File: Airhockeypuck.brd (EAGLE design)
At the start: 80 x 80 mm, 22 parts, among them J1 USB-MB-H

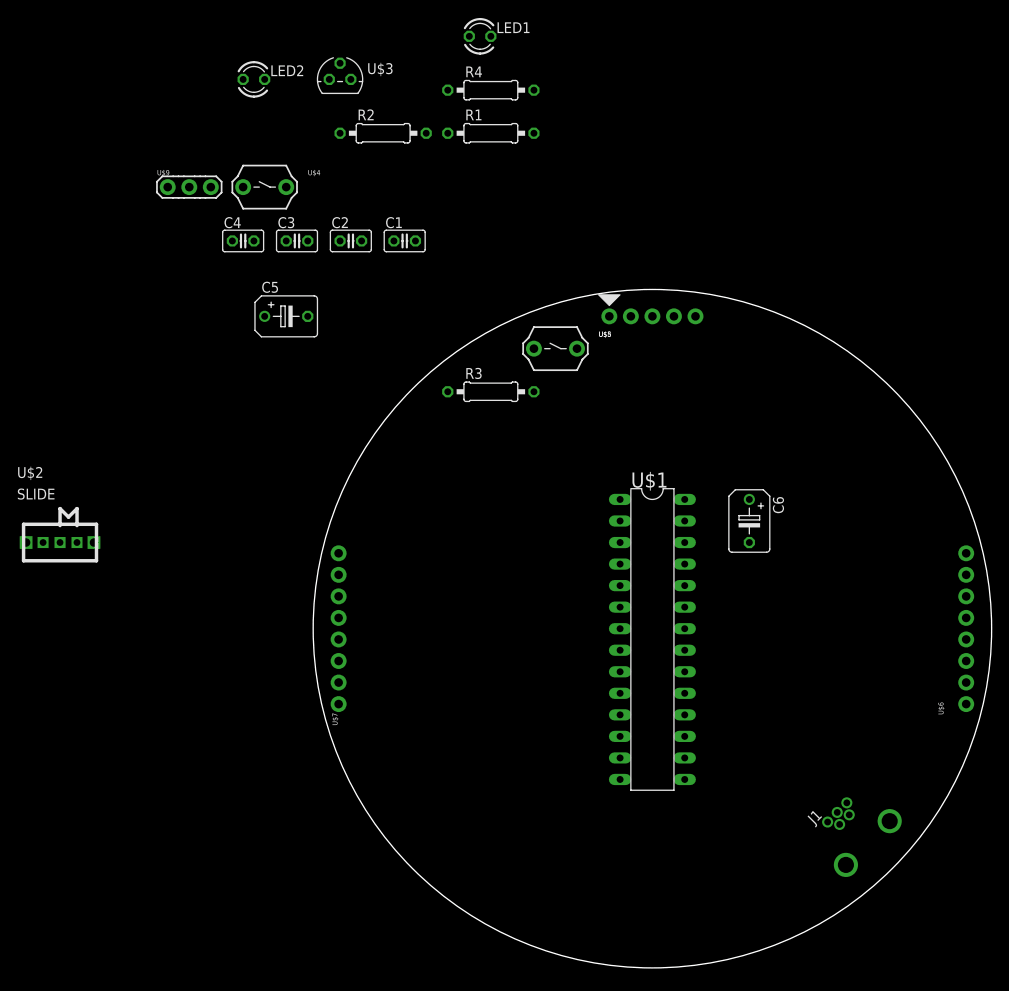
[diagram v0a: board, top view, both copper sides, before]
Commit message: Created IMU part and added into PCB design
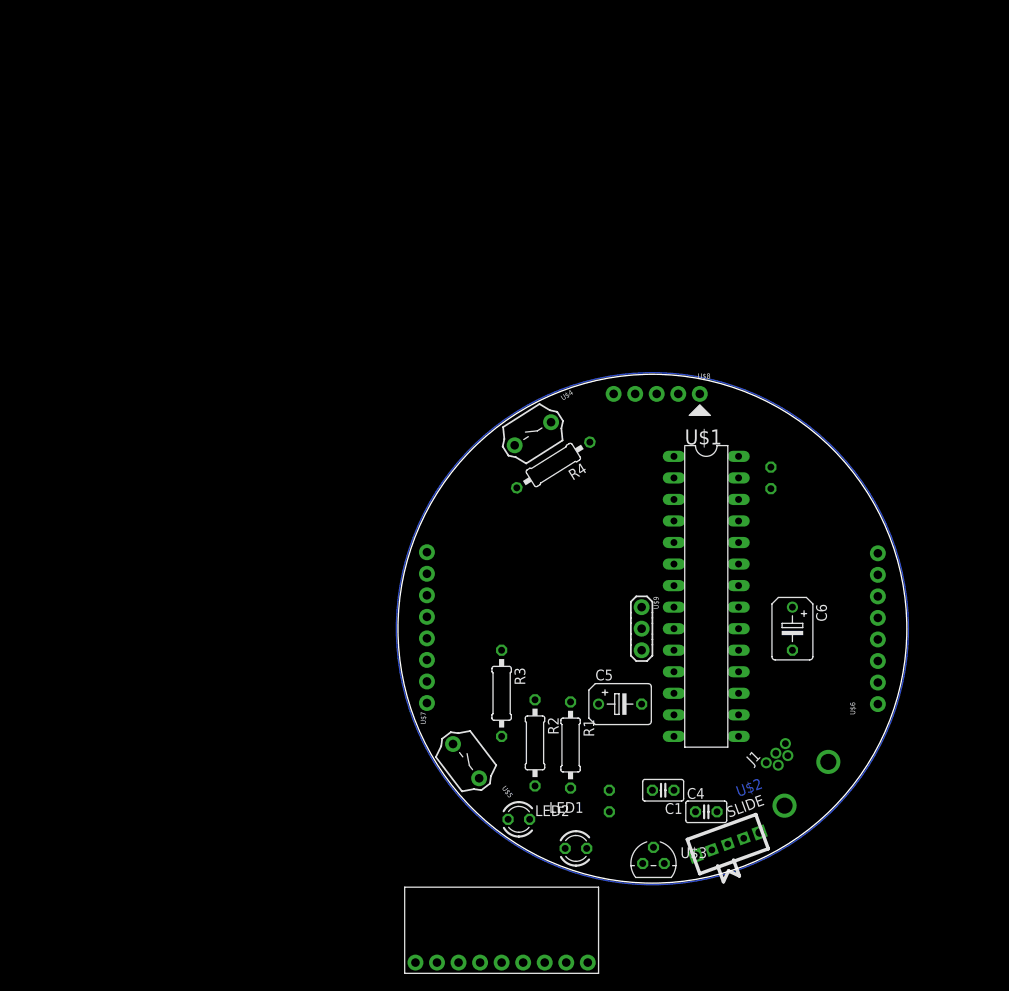
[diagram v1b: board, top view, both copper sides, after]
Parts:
- added U$10: IMU, MEE_433:IMU
- moved U$3 99.6 mm to (0.13, -26.4)
- moved LED1 96.4 mm to (-9.02, -24.6)
- moved LED2 92.7 mm to (-15.7, -21.2)
- moved C4 86.7 mm to (6.35, -20.3)
- moved U$2 86.4 mm to (8.89, -24.1), turned to 200 degrees
- moved U$9 74.5 mm to (-1.27, 1.27), turned to 270 degrees
- moved R2 74.1 mm to (-13.8, -12.2), turned to 270 degrees
- moved R1 72.7 mm to (-9.65, -12.4), turned to 270 degrees
- moved C2 72.7 mm to (-5.08, -19.1), flipped to the bottom, turned to 90 degrees
- moved C1 71.6 mm to (1.27, -17.8), turned to 180 degrees
- moved C3 62.5 mm to (14.0, 19.1), flipped to the bottom, turned to 270 degrees
- moved C5 60.3 mm to (-3.81, -7.62)
- moved U$5 49.8 mm to (-22.0, -14.4), turned to 307.3 degrees
- moved R4 44.8 mm to (-11.7, 20.6), turned to 212 degrees
- moved U$4 43.0 mm to (-14.1, 24.3), turned to 32.4 degrees
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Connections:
- net +5V: now also U$2.2
- net N$1: now also U$2.3; no longer U$2.2
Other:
- board size 80 x 80 mm -> 60 x 60 mm

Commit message: minor edits
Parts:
- moved U$10 51.1 mm to (-1.02, 5.33), turned to 90 degrees
- moved U$9 1.27 mm to (-1.27, 0.00)
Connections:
- net +3V3: now also U$10.2.
- net B2: now also U$10.4.
- net B3: now also U$10.5.
- net GND: now also U$10.3.
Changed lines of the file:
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@@
 <attribute name="VALUE" x="6.858" y="32.258" size="0.6096" layer="27" font="vector" ratio="20" rot="R180"/>
 </element>
-<element name="U$9" library="MEE_433" package="OSC" value="8MHz" x="-1.27" y="1.27" smashed="yes" rot="R270">
-<attribute name="NAME" x="0.127" y="5.08" size="0.6096" layer="25" font="vector" ratio="20" rot="R270"/>
-<attribute name="VALUE" x="-3.302" y="5.08" size="0.6096" layer="27" font="vector" ratio="20" rot="R270"/>
+<element name="U$9" library="MEE_433" package="OSC" value="8MHz" x="-1.27" y="0" smashed="yes" rot="R270">
+<attribute name="NAME" x="0.127" y="3.81" size="0.6096" layer="25" font="vector" ratio="20" rot="R270"/>
+<attribute name="VALUE" x="-3.302" y="3.81" size="0.6096" layer="27" font="vector" ratio="20" rot="R270"/>
 </element>
-<element name="U$10" library="MEE_433" package="IMU" value="IMU" x="-27.94" y="-38.1" smashed="yes"/>
+<element name="U$10" library="MEE_433" package="IMU" value="IMU" x="-1.016" y="5.334" smashed="yes" rot="R90"/>
 </elements>
 <signals>
@@
 <contactref element="U$6" pad="1"/>
 <contactref element="U$7" pad="1"/>
+<contactref element="U$10" pad="3."/>
 <wire x1="-26.586" y1="-7.493" x2="-20.4317875" y2="-16.3715" width="0" layer="19" extent="1-1"/>
 <wire x1="-13.843" y1="-7.112" x2="-20.4317875" y2="-16.3715" width="0" layer="19" extent="1-1"/>
 <wire x1="-9.652" y1="-7.366" x2="-13.843" y2="-7.112" width="0" layer="19" extent="1-1"/>
 <wire x1="-1.27" y1="-7.62" x2="-9.652" y2="-7.366" width="0" layer="19" extent="1-1"/>
-<wire x1="-1.27" y1="1.27" x2="-1.27" y2="-7.62" width="0" layer="19" extent="1-1"/>
-<wire x1="2.54" y1="3.81" x2="-1.27" y2="1.27" width="0" layer="19" extent="1-1"/>
+<wire x1="-1.27" y1="0" x2="-1.27" y2="-7.62" width="0" layer="19" extent="1-1"/>
+<wire x1="2.54" y1="3.81" x2="-1.27" y2="0" width="0" layer="19" extent="1-1"/>
+<wire x1="-1.016" y1="10.414" x2="2.54" y2="3.81" width="0" layer="19" extent="1-1"/>
 <wire x1="10.16" y1="-1.27" x2="2.54" y2="3.81" width="0" layer="19" extent="1-1"/>
 <wire x1="16.51" y1="-1.27" x2="10.16" y2="-1.27" width="0" layer="19" extent="1-1"/>
@@
 <wire x1="-1.143" y1="-26.416" x2="0" y2="-17.78" width="0" layer="19" extent="1-1"/>
 <wire x1="26.586" y1="-7.62" x2="16.51" y2="-1.27" width="0" layer="19" extent="1-1"/>
-<wire x1="10.16" y1="19.05" x2="2.54" y2="3.81" width="0" layer="19" extent="1-1"/>
+<wire x1="10.16" y1="19.05" x2="-1.016" y2="10.414" width="0" layer="19" extent="1-1"/>
 <wire x1="13.97" y1="17.78" x2="10.16" y2="19.05" width="0" layer="19" extent="1-1"/>
 <wire x1="0.508" y1="28.956" x2="10.16" y2="19.05" width="0" layer="19" extent="1-1"/>
@@
 <contactref element="R3" pad="1"/>
 <contactref element="U$7" pad="2"/>
+<contactref element="U$10" pad="2."/>
 <wire x1="10.16" y1="21.59" x2="13.97" y2="20.32" width="0" layer="19" extent="1-1"/>
 <wire x1="3.048" y1="28.956" x2="10.16" y2="21.59" width="0" layer="19" extent="1-1"/>
@@
 <wire x1="10.16" y1="8.89" x2="13.97" y2="20.32" width="0" layer="19" extent="1-1"/>
 <wire x1="16.51" y1="3.81" x2="10.16" y2="8.89" width="0" layer="19" extent="1-1"/>
-<wire x1="2.54" y1="-8.89" x2="16.51" y2="3.81" width="0" layer="19" extent="1-1"/>
+<wire x1="-1.016" y1="7.874" x2="10.16" y2="8.89" width="0" layer="19" extent="1-1"/>
+<wire x1="2.54" y1="-8.89" x2="-1.016" y2="7.874" width="0" layer="19" extent="1-1"/>
 <wire x1="2.54" y1="-17.78" x2="2.54" y2="-8.89" width="0" layer="19" extent="1-1"/>
 <wire x1="-5.08" y1="-20.32" x2="2.54" y2="-17.78" width="0" layer="19" extent="1-1"/>
 <wire x1="-10.287" y1="-24.638" x2="-5.08" y2="-20.32" width="0" layer="19" extent="1-1"/>
 <wire x1="1.397" y1="-26.416" x2="2.54" y2="-17.78" width="0" layer="19" extent="1-1"/>
-<wire x1="-17.78" y1="-1.27" x2="2.54" y2="-8.89" width="0" layer="19" extent="1-1"/>
+<wire x1="-17.78" y1="-1.27" x2="-1.016" y2="7.874" width="0" layer="19" extent="1-1"/>
 <wire x1="-26.586" y1="-4.953" x2="-17.78" y2="-1.27" width="0" layer="19" extent="1-1"/>
 </signal>
@@
 <contactref element="U$9" pad="1"/>
 <contactref element="U$1" pad="9"/>
-<wire x1="2.54" y1="1.27" x2="-1.27" y2="3.81" width="0" layer="19" extent="1-1"/>
+<wire x1="2.54" y1="1.27" x2="-1.27" y2="2.54" width="0" layer="19" extent="1-1"/>
 </signal>
 <signal name="N$6">
 <contactref element="U$9" pad="3"/>
 <contactref element="U$1" pad="10"/>
-<wire x1="-1.27" y1="-1.27" x2="2.54" y2="-1.27" width="0" layer="19" extent="1-1"/>
+<wire x1="2.54" y1="-1.27" x2="-1.27" y2="-2.54" width="0" layer="19" extent="1-1"/>
 </signal>
 <signal name="+5V">
@@
 <contactref element="U$1" pad="6"/>
 <contactref element="U$7" pad="6"/>
-<wire x1="2.54" y1="8.89" x2="-26.586" y2="5.207" width="0" layer="19" extent="1-1"/>
+<contactref element="U$10" pad="4."/>
+<wire x1="-1.016" y1="12.954" x2="-26.586" y2="5.207" width="0" layer="19" extent="1-1"/>
+<wire x1="2.54" y1="8.89" x2="-1.016" y2="12.954" width="0" layer="19" extent="1-1"/>
 </signal>
 <signal name="B3">
 <contactref element="U$1" pad="7"/>
 <contactref element="U$7" pad="5"/>
-<wire x1="2.54" y1="6.35" x2="-26.586" y2="2.667" width="0" layer="19" extent="1-1"/>
+<contactref element="U$10" pad="5."/>
+<wire x1="-1.016" y1="15.494" x2="-26.586" y2="2.667" width="0" layer="19" extent="1-1"/>
+<wire x1="2.54" y1="6.35" x2="-1.016" y2="15.494" width="0" layer="19" extent="1-1"/>
 </signal>
 <signal name="B4/USER">

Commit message: minor edits
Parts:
- added U$11: HC-08, MEE_433:HC-08
- U$6, U$7: value CONN_08 -> DRV8835; device MEE_433:1X08 -> MEE_433:DRV8835
- moved U$6 40.3 mm to (-12.7, 1.27)
- moved U$7 40.3 mm to (12.7, 1.27), turned to 270 degrees
- moved C6 32.4 mm to (10.2, 33.0), turned to 180 degrees
- moved C3 31.2 mm to (-14.0, 33.0), turned to 180 degrees
- moved C5 26.2 mm to (20.3, -17.8), turned to 180 degrees
- moved U$1 20.9 mm to (1.27, 25.4), turned to 0 degrees
- moved U$9 19.3 mm to (6.35, 17.8), turned to 0 degrees
- moved U$2 19.0 mm to (27.8, -22.1), turned to 223.9 degrees
- moved U$10 17.0 mm to (8.64, -8.64), turned to 180 degrees
- moved U$3 16.1 mm to (15.4, -31.5)
- moved C1 15.3 mm to (15.2, -24.1)
- moved C4 15.3 mm to (20.3, -26.7), turned to 90 degrees
- moved C2 15.3 mm to (10.2, -20.3), turned to 270 degrees
- moved J1 14.9 mm to (32.1, -11.9), turned to 147.9 degrees
- moved R3 12.7 mm to (-25.4, -16.5)
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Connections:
- new net N$10: U$6.10.BENABLE
- new net N$11: U$6.11.BPHASE
- new net N$12: U$6.12.AENABLE
- new net N$13: U$6.13.APHASE
- new net N$14: U$11.4.RX
- new net N$16: U$7.10.BENABLE
- new net N$17: U$7.11.BPHASE
- new net N$18: U$7.12.AENABLE
- new net N$19: U$7.13.APHASE
- new net N$3: U$11.1.VCC
- new net N$9: U$11.3.TX
- net +3V3: now also U$6.9.VCC, U$7.9.VCC; no longer U$7.2
- net +5V: now also U$2.1.+5V; no longer U$2.1, U$6.2
- net A0: no longer U$7.8
- net A1: no longer U$7.7
- net A4/LED: no longer U$7.3
- net B13: no longer U$6.6
- net B14: no longer U$6.7
- net B15: no longer U$6.8
- net B2: no longer U$7.6
- net B3: no longer U$7.5
- net B4/USER: no longer U$7.4
- net B7: no longer U$6.3
- net B8: no longer U$6.4
- net B9: no longer U$6.5
- net GND: now also U$11.2.GND, U$6.8.GND, U$7.8.GND; no longer U$6.1, U$7.1
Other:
- board size 60 x 60 mm -> 80 x 80 mm

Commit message: minor edits
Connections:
- net N$18 renamed A4
- removed net N$10: U$6.10.BENABLE
- removed net N$11: U$6.11.BPHASE
- removed net N$12: U$6.12.AENABLE
- removed net N$13: U$6.13.APHASE
- removed net N$14: U$11.4.RX
- removed net N$16: U$7.10.BENABLE
- removed net N$17: U$7.11.BPHASE
- removed net N$19: U$7.13.APHASE
- removed net N$9: U$11.3.TX
- net A1: now also U$11.3.TX
- net B14: now also U$11.4.RX
- net B15: now also U$6.10.BENABLE
- net B7: now also U$6.11.BPHASE, U$6.13.APHASE, U$7.11.BPHASE, U$7.13.APHASE
- net B8: now also U$6.12.AENABLE
- net B9: now also U$7.10.BENABLE
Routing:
- net +3V3: track 0.00 -> 229.2 mm
- net +5V: track 0.00 -> 86.9 mm
- net MCLR: track 0.00 -> 56.3 mm
- net USBID: track 0.00 -> 40.3 mm
- net N$1: track 0.00 -> 15.8 mm
- net N$6: track 0.00 -> 4.34 mm
- net N$2: track 0.00 -> 4.34 mm
- added copper zone on layer 16, net GND

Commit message: completed connections
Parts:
- moved U$11 63.7 mm to (-15.1, 35.7), turned to 113.9 degrees
- moved C6 54.1 mm to (19.1, -20.3)
- moved C5 53.8 mm to (2.54, 33.0)
- moved C3 6.35 mm to (-7.62, 33.0)
- moved R4 1.27 mm to (-23.1, 23.1)
- moved U$4 1.27 mm to (-24.3, 28.1), turned to 41.9 degrees
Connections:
- removed net A4/LED: LED2.A, U$1.12
- net A4: now also U$1.12
- net B7: now also LED2.A
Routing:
- net B7: track 0.00 -> 158.9 mm, vias 0 -> 15
- net D+: track 0.00 -> 77.5 mm, vias 0 -> 6
- net D-: track 0.00 -> 74.3 mm, vias 0 -> 8
- net B8: track 0.00 -> 59.0 mm, vias 0 -> 4
- net B9: track 0.00 -> 54.3 mm, vias 0 -> 4
- net B4/USER: track 0.00 -> 53.8 mm, vias 0 -> 2
- net A4: track 0.00 -> 48.6 mm, vias 0 -> 4
- net MCLR: track 56.3 -> 97.5 mm, vias 0 -> 4
- net B3: track 0.00 -> 35.7 mm, vias 0 -> 2
- net B2: track 0.00 -> 35.3 mm
- net B15: track 0.00 -> 32.9 mm, vias 0 -> 2
- net +3V3: track 229.2 -> 252.2 mm, vias 0 -> 8
- net PGD: track 0.00 -> 18.6 mm, vias 0 -> 2
- net A1: track 0.00 -> 17.7 mm, vias 0 -> 2
- net PGC: track 0.00 -> 17.1 mm
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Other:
- outline, holes or cut-outs redrawn

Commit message: minor edits
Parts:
- flipped C2 to the top
- flipped C3 to the top
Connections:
- new net N$8: C4.1, U$2.2, U$3.2
- net +5V: no longer C4.1, U$2.2, U$3.2
- net GND: now also J1.GND
- net USBID: no longer J1.GND
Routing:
- net +5V: track 86.9 -> 68.1 mm
- net N$8: track 0.00 -> 16.9 mm
- net +3V3: track 252.2 -> 255.8 mm, vias 8 -> 11
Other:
- board text added: "+"
- board text added: "AENABLE"
- board text added: "AOUT1"
- board text added: "AOUT2"
- board text added: "APHASE"
- board text added: "BENABLE"
- board text added: "BOUT1"
- board text added: "BOUT2"
- board text added: "BPHASE"
- board text added: "Devdhark Dhanvink MEE499"
